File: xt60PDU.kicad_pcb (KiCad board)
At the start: 2 copper layers, 50 x 16 mm, 7 parts, among them J1 Conn_01x02_Pin, J2 Conn_01x02_Socket, J3 Conn_01x02_Socket, J4 Conn_01x02_Socket, J5 Conn_01x02_Socket

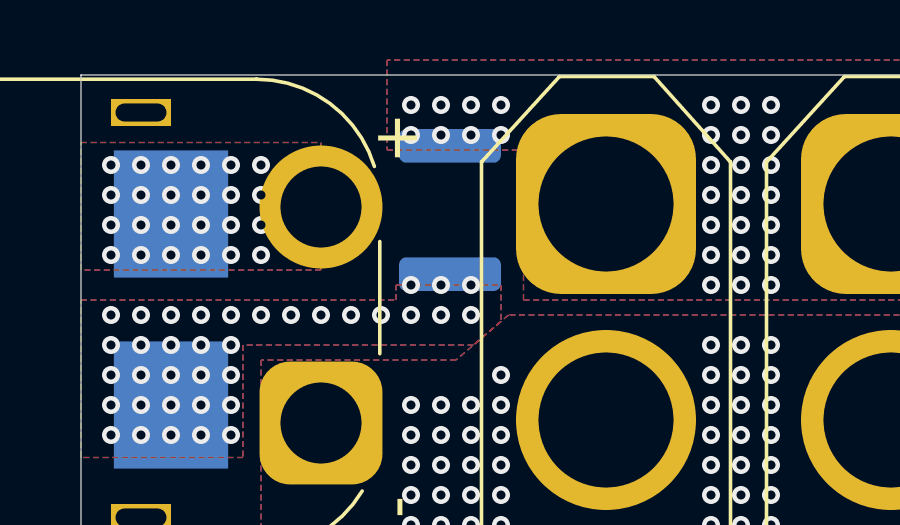
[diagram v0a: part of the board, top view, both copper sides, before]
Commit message: Replace the 1812 PTC footprint with one that is shorted by default
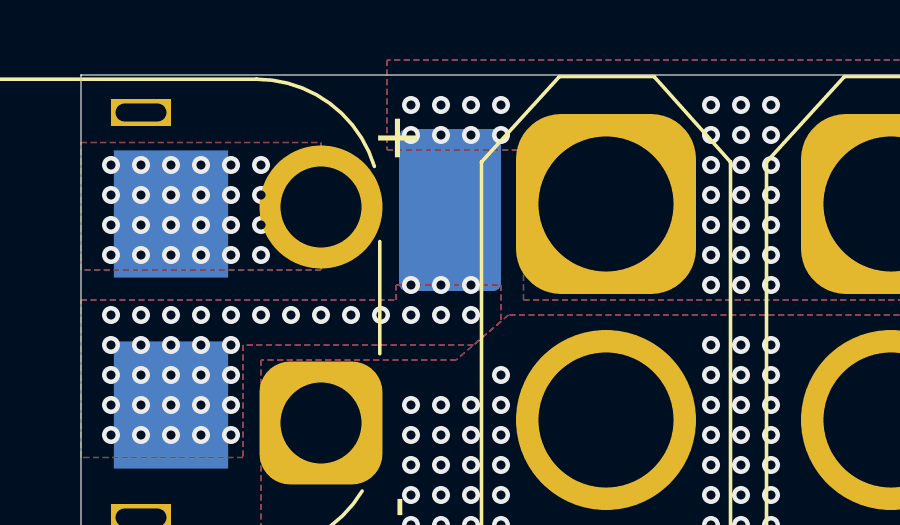
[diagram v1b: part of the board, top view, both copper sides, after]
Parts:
- F2: footprint Fuse:Fuse_1812_4532Metric -> SMD:SolderJumper-2_1812_Bridged_3.2mm
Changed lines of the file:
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@@
 		)
 	)
-	(footprint "Fuse:Fuse_1812_4532Metric"
+	(footprint "SMD:SolderJumper-2_1812_Bridged_3.2mm"
 		(layer "B.Cu")
 		(at 62.3 54.5 90)
-		(descr "Fuse SMD 1812 (4532 Metric), square (rectangular) end terminal, IPC-7351 nominal, (Body size source: https://www.nikhef.nl/pub/departments/mt/projects/detectorR_D/dtddice/ERJ2G.pdf), generated with kicad-footprint-generator")
-		(tags "fuse")
+		(descr "Bridged Fuse SMD 1812 (4532 Metric), square (rectangular) end terminal, IPC-7351 nominal, (Body size source: https://www.nikhef.nl/pub/departments/mt/projects/detectorR_D/dtddice/ERJ2G.pdf), generated with kicad-footprint-generator")
+		(tags "net tie solder jumper bridged")
 		(property "Reference" "F2"
-			(at 0 2.65 90)
+			(at 0 2.65 270)
 			(layer "B.SilkS")
 			(hide yes)
@@
 		)
 		(property "Value" "Polyfuse"
-			(at 0 -2.65 90)
+			(at 0 -2.65 270)
 			(layer "B.Fab")
 			(hide yes)
@@
 		)
 		(property "Datasheet" ""
-			(at 0 0 90)
+			(at 0 0 270)
 			(layer "B.Fab")
 			(hide yes)
@@
 		)
 		(property "Description" "Resettable fuse, polymeric positive temperature coefficient"
-			(at 0 0 90)
+			(at 0 0 270)
 			(layer "B.Fab")
 			(hide yes)
@@
 		(sheetname "/")
 		(sheetfile "xt60PDU.kicad_sch")
-		(attr smd)
+		(zone_connect 1)
+		(attr smd exclude_from_pos_files)
+		(net_tie_pad_groups "1, 2")
+		(fp_poly
+			(pts
+				(xy 1.8 1.7) (xy -1.8 1.7) (xy -1.8 -1.7) (xy 1.8 -1.7)
+			)
+			(stroke
+				(width 0)
+				(type solid)
+			)
+			(fill yes)
+			(layer "B.Cu")
+		)
 		(fp_line
 			(start -1.386252 -1.71)
@@
 		)
 		(fp_text user "${REFERENCE}"
-			(at 0 0 90)
+			(at 0 0 270)
 			(layer "B.Fab")
 			(effects
@@
 			(net 4 "/VFUSE")
 			(pintype "passive")
+			(zone_connect 2)
 		)
 		(pad "2" smd roundrect
@@
 			(net 2 "/VCC")
 			(pintype "passive")
+			(zone_connect 2)
 		)
 		(embedded_fonts no)
